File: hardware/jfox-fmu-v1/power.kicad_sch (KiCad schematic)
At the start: 7 parts, among them U20 LTC4417CGN, U21 TPS62130, U22 AP2112K-3.3, U23 AP22804AW5, U24 AP22804AW5, U25 AP22804AW5, U26 AP22804AW5

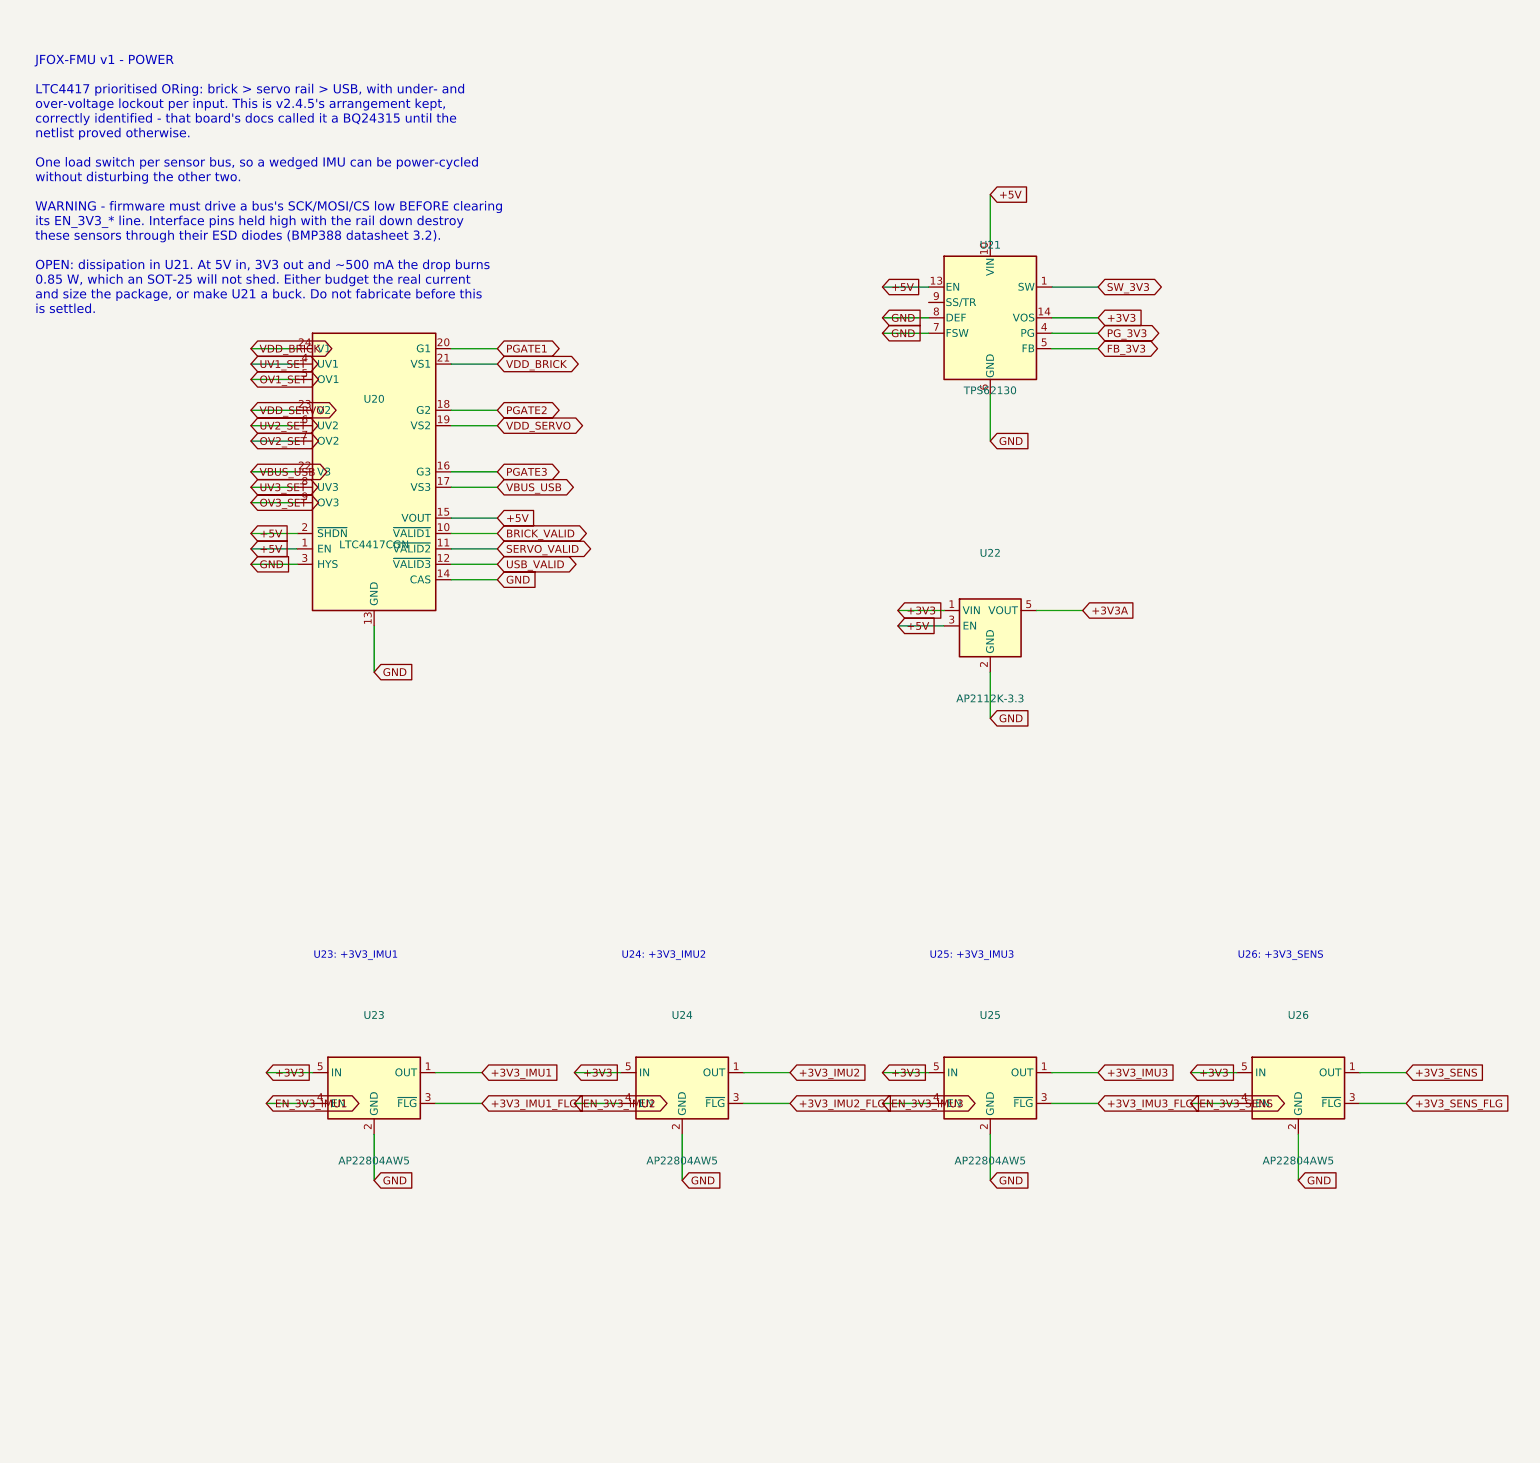
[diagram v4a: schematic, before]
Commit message: A4 title-blocked sheets, and the 25 power pins that were never wired
Every sheet now carries a title block naming JFOX Aircraft Co., Ltd., with a
per-sheet title, revision, date and the notes that used to float as loose text.

A4 PORTRAIT, not landscape, and not by preference. The STM32H753IITx symbol is
a single unit - KiCad's library gives it only _0_1 body and _1_1 pin
sub-symbols, so it cannot be split across pages - and its 176 pins span
231.1 mm. A4 landscape offers about 180 mm of usable height and would cut the
MCU in half. Portrait offers 237 mm. The part fits with 2 mm to spare, which
is why the page margin is 2 mm: it is the largest margin that still holds an
LQFP176, not a number chosen for looks.

The frame geometry was measured, not assumed - an empty A4 portrait sheet
plotted through kicad-cli, frame read off the SVG at 12,12 -> 198,285 with the
title block claiming x >= 90, y >= 253.

Three defects the work surfaced, in rising order of how much they mattered:

Every sheet had content at negative coordinates, off the page entirely, where
KiCad edits it happily and the plotter crops it away. Nothing had complained
because nothing was looking. fit() now translates each sheet into the drawable
area and refuses - loudly - to emit one that does not fit, because a schematic
that is silently cropped lies about the board.

fit() then passed the power sheet while its rightmost label sat 8.6 mm past
the frame. A global label's angle is the direction its CONNECTION faces, so
the text runs the opposite way; reading it the intuitive way put every
estimated extent on the wrong side of its anchor. That is worse than not
estimating: it reports "inside the frame" precisely when labels hang off it.
Caught by measuring KiCad's own plotted geometry instead of trusting the
estimate - which is what check_fmu_sheets.py now does on every sheet, with
--exclude-drawing-sheet so only the circuit is measured.

And centring the sheets by (SAFE_W - w) / 2 shifted every wire off th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
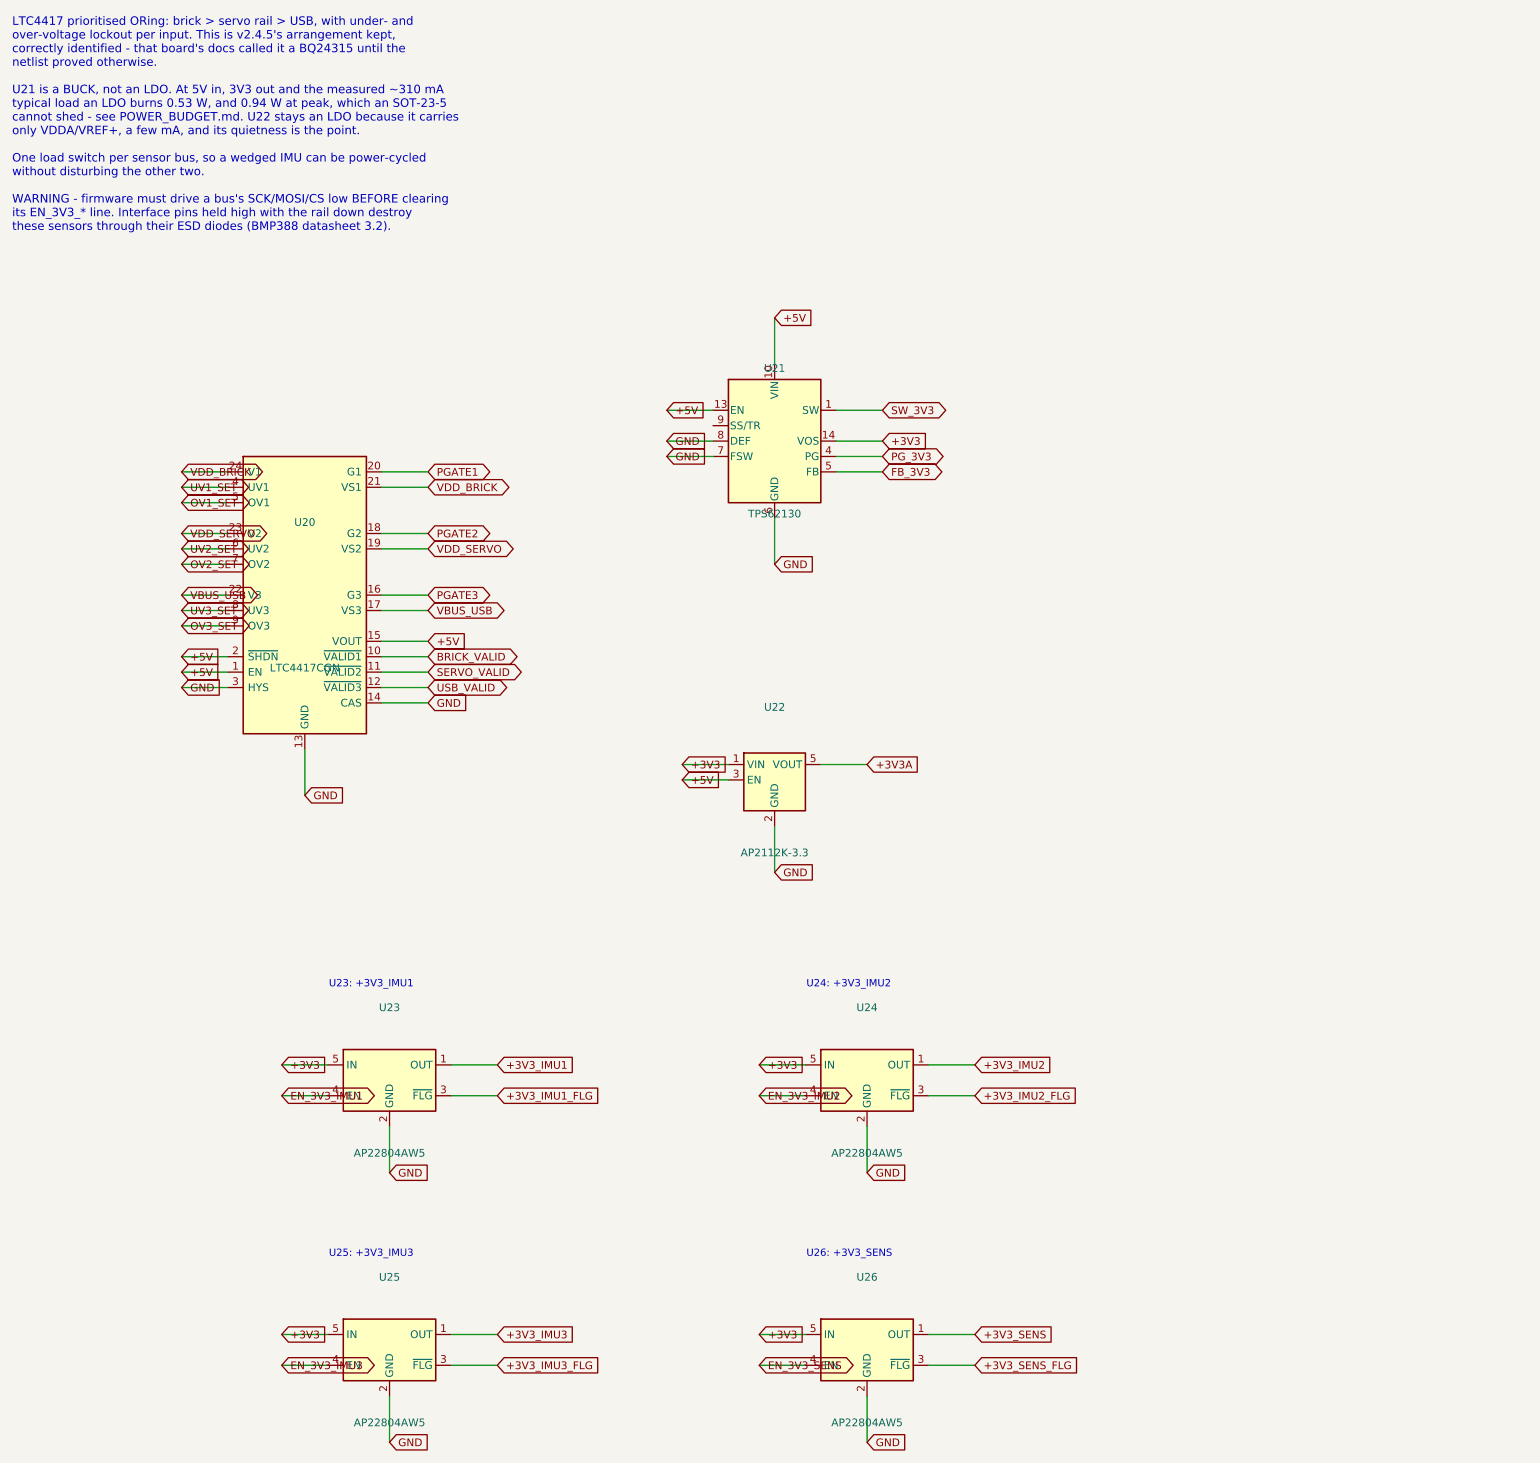
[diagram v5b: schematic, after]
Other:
- note added: "LTC4417 prioritised ORing: brick > servo rail > USB, with under- and over-voltage lockout per input. This is v2.4.5's arrangement kept, correctly identified - that board's docs called it a BQ24315 until the netlist proved otherwise. U21 is a BUCK, not an LDO. At 5V in, 3V3 out and the measured ~310 mA typical load an LDO burns 0.53 W, and 0.94 W at peak, which an SOT-23-5 cannot shed - see POWER_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"
- note removed: "JFOX-FMU v1 - POWER LTC4417 prioritised ORing: brick > servo rail > USB, with under- and over-voltage lockout per input. This is v2.4.5's arrangement kept, correctly identified - that board's docs called it a BQ24315 until the netlist proved otherwise. One load switch per sensor bus, so a wedged IMU can be power-cycled without disturbing the other two. WARNING - firmware must drive a bus's SCK/MO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"
- company: (none) -> JFOX Aircraft Co., Ltd.
- title: (none) -> Power

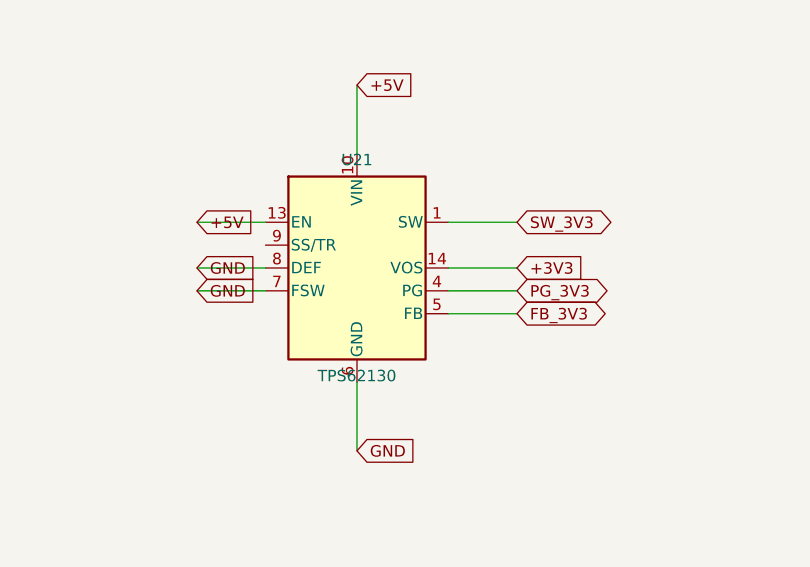
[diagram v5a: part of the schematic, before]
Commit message: U21 was set to 2.24 V, not 3.3 V
The 3V3 rail's regulator was an adjustable TPS62130 with a 180k/100k feedback
divider, carried in the schematic as "a starting point from the datasheet's
3V3 example". It was not a starting point. The TPS62130 regulates FB to 800 mV
(SLVSAG7F 9.2.2.1, equation 6), so 180k over 100k sets

    0.8 x (1 + 180/100) = 2.24 V

onto a net named +3V3. For 3.3 V the top resistor needed to be 312.5k.

Nothing caught this and nothing could have. ERC checks connectivity, not
arithmetic; the net was named +3V3 and every part was correctly connected to
it, so every structural check passed on a board that would have browned out
the STM32H753 and undervolted all three IMUs. The whole error was numbers,
and numbers were what nothing was looking at.

U21 becomes a TPS62132 - the fixed 3.3 V member of the same family, in the
same package, with a KiCad symbol already present. That removes the divider
instead of correcting it: two fewer parts, no divider tolerance stacking on
the reference, and the output voltage becomes a property of the ordering code
rather than something a resistor substitution can silently change.

Three parts the design was missing, all from the datasheet's own typical
application (figure 9-1): C28 100n on AVIN, C29 3n3 setting the soft-start
ramp, and R3 100k pulling up PG - which is open drain and was wired to a net
nothing on the board could drive.

L1 2u2 and C27 22u turn out to have been right all along, and now say why:
table 9-2 marks 2.2uH/22uF as the standard, recommended combination. FSW low
is 2.5 MHz for smallest size and lowest ripple; DEF low is nominal output; FB
goes to AGND as the datasheet asks for fixed versions.

check_fmu_schematic.py grows an eighth check: every rail must produce the
voltage its name claims. Fixed parts are verified by ordering code, adjustable
ones by computing Vfb x (1 + Rtop/Rbot) from the BOM values. Negative-tested
by restoring the 180k/100k divider, which it reports as 2.24 V, and by the
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
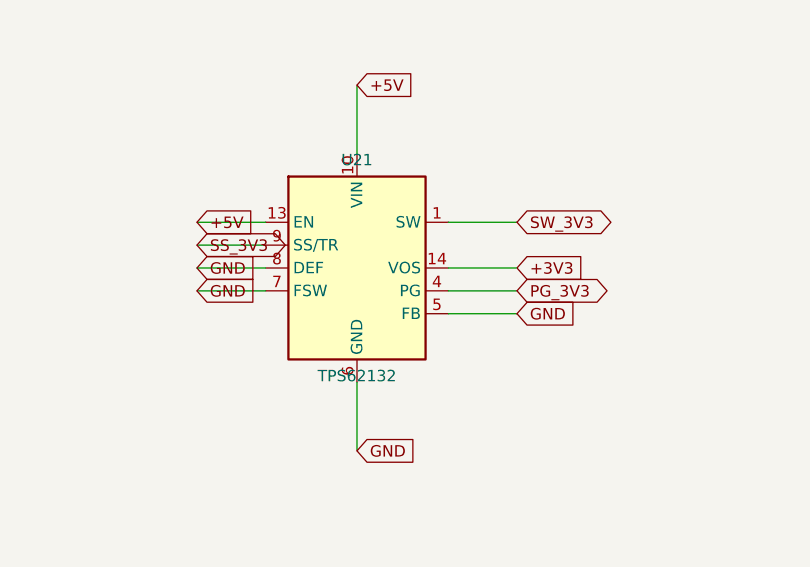
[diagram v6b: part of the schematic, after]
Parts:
- removed U21: TPS62130, symbol Regulator_Switching:TPS62130
- added U21: TPS62132, symbol Regulator_Switching:TPS62132
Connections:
- net +3V3: now also U21.14 (VOS)
- net +5V: now also U21.10 (VIN), U21.11 (VIN), U21.12 (VIN), U21.13 (EN)
- net GND: now also U21.15 (GND), U21.16 (GND), U21.17 (GND), U21.5 (FB), U21.6 (GND), U21.7 (FSW), U21.8 (DEF)
- net PG_3V3: now also U21.4 (PG)
- net SW_3V3: now also U21.1 (SW), U21.2 (SW), U21.3 (SW)
- new net SS_3V3: U21.9 (SS/TR)
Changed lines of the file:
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@@
 		(instances
 			(project "jfox-fmu"
-				(path "/002827d4-4ac0-46d7-9ffb-9b156823eeb4"
+				(path "/d1e8a681-6ee5-4e7f-b035-aebe49eafd3e"
 					(reference "U20")
 					(unit 1)
@@
 	)
 	(symbol
-		(lib_id "Regulator_Switching:TPS62130")
+		(lib_id "Regulator_Switching:TPS62132")
 		(at 142.24 83.82 0)
 		(unit 1)
@@
 		)
 		)
-		(property "Value" "TPS62130"
+		(property "Value" "TPS62132"
 			(at 142.24 95.82 0)
 			(effects
@@
 		(instances
 			(project "jfox-fmu"
-				(path "/002827d4-4ac0-46d7-9ffb-9b156823eeb4"
+				(path "/d1e8a681-6ee5-4e7f-b035-aebe49eafd3e"
 					(reference "U21")
 					(unit 1)
@@
 		)
 	)
-	(global_label "FB_3V3"
-		(shape bidirectional)
+	(global_label "GND"
+		(shape input)
 		(at 160.02 88.9 180)
 		(fields_autoplaced yes)
@@
 		(shape input)
 		(at 124.46 83.82 0)
+		(fields_autoplaced yes)
+		(effects
+			(font
+				(size 1.27 1.27)
+			)
+			(justify left)
+		)
+	)
+	(wire
+		(pts
+			(xy 132.08 81.28) (xy 124.46 81.28)
+		)
+		(stroke
+			(width 0)
+			(type default)
+		)
+	)
+	(global_label "SS_3V3"
+		(shape bidirectional)
+		(at 124.46 81.28 0)
 		(fields_autoplaced yes)
 		(effects
@@
 		(instances
 			(project "jfox-fmu"
-				(path "/002827d4-4ac0-46d7-9ffb-9b156823eeb4"
+				(path "/d1e8a681-6ee5-4e7f-b035-aebe49eafd3e"
 					(reference "U22")
 					(unit 1)
@@
 		(instances
 			(project "jfox-fmu"
-				(path "/002827d4-4ac0-46d7-9ffb-9b156823eeb4"
+				(path "/d1e8a681-6ee5-4e7f-b035-aebe49eafd3e"
 					(reference "U23")
 					(unit 1)
@@
 		(instances
 			(project "jfox-fmu"
-				(path "/002827d4-4ac0-46d7-9ffb-9b156823eeb4"
+				(path "/d1e8a681-6ee5-4e7f-b035-aebe49eafd3e"
 					(reference "U24")
 					(unit 1)
@@
 		(instances
 			(project "jfox-fmu"
-				(path "/002827d4-4ac0-46d7-9ffb-9b156823eeb4"
+				(path "/d1e8a681-6ee5-4e7f-b035-aebe49eafd3e"
 					(reference "U25")
 					(unit 1)
@@
 		(instances
 			(project "jfox-fmu"
-				(path "/002827d4-4ac0-46d7-9ffb-9b156823eeb4"
+				(path "/d1e8a681-6ee5-4e7f-b035-aebe49eafd3e"
 					(reference "U26")
 					(unit 1)
